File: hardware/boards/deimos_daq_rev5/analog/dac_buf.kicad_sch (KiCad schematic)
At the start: 3 parts, among them IC53001 INA826AIDR

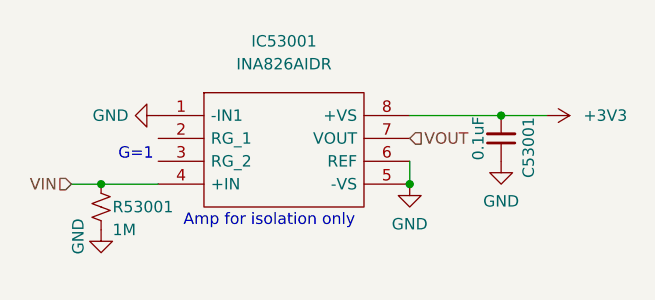
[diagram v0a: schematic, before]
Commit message: put +/12V on all inamps. add 3.3V zener behind first resistor of each filter.
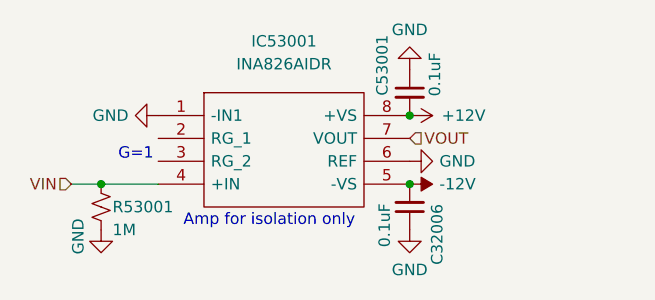
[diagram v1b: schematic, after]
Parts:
- added C32006: 0.1uF, Capacitor_SMD:C_0402_1005Metric, symbol Device:C_Small
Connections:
- net GND: now also C32006.1; no longer IC53001.5 (-VS)
- net +3V3 renamed +12V
- new net -12V: C32006.2, IC53001.5 (-VS)
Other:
- moved on the sheet: C53001

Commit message: add stabilizing integrator to current sinks
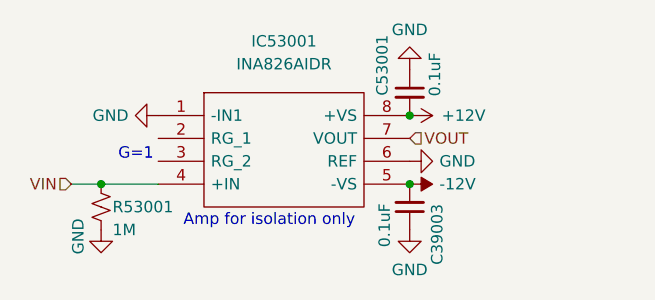
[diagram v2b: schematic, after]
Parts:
- renumbered C32006 to C39003
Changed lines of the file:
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@@
 		(on_board yes)
 		(dnp no)
-		(property "Reference" "C32006"
+		(property "Reference" "C39003"
 			(at 158.242 111.506 90)
 			(effects
@@
 		(dnp no)
 		(fields_autoplaced yes)
-		(property "Reference" "#PWR32013"
+		(property "Reference" "#PWR39013"
 			(at 155.194 117.348 0)
 			(effects

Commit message: restore rev5 and make this rev rev6
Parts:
- removed C39003: 0.1uF, Capacitor_SMD:C_0402_1005Metric, symbol Device:C_Small
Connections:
- net -12V is gone; now on net GND: IC53001.5 (-VS)
- net +12V renamed +3V3
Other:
- moved on the sheet: C53001
